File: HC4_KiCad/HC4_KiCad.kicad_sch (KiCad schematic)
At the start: 17 parts, among them IC1 KM62256CLP, IC2 ROM, J1 Power, J2 ~{CE}_EXT, SW1 SW_SPDT_312

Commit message: 基板ぬ
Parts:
- IC1: footprint Package_DIP:DIP-28_W15.24mm -> Package_SO:SOP-28_8.4x18.16mm_P1.27mm
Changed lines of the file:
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@@
 			)
 		)
-		(property "Footprint" "Package_DIP:DIP-28_W15.24mm"
+		(property "Footprint" "Package_SO:SOP-28_8.4x18.16mm_P1.27mm"
 			(at 48.26 85.09 0)
 			(effects

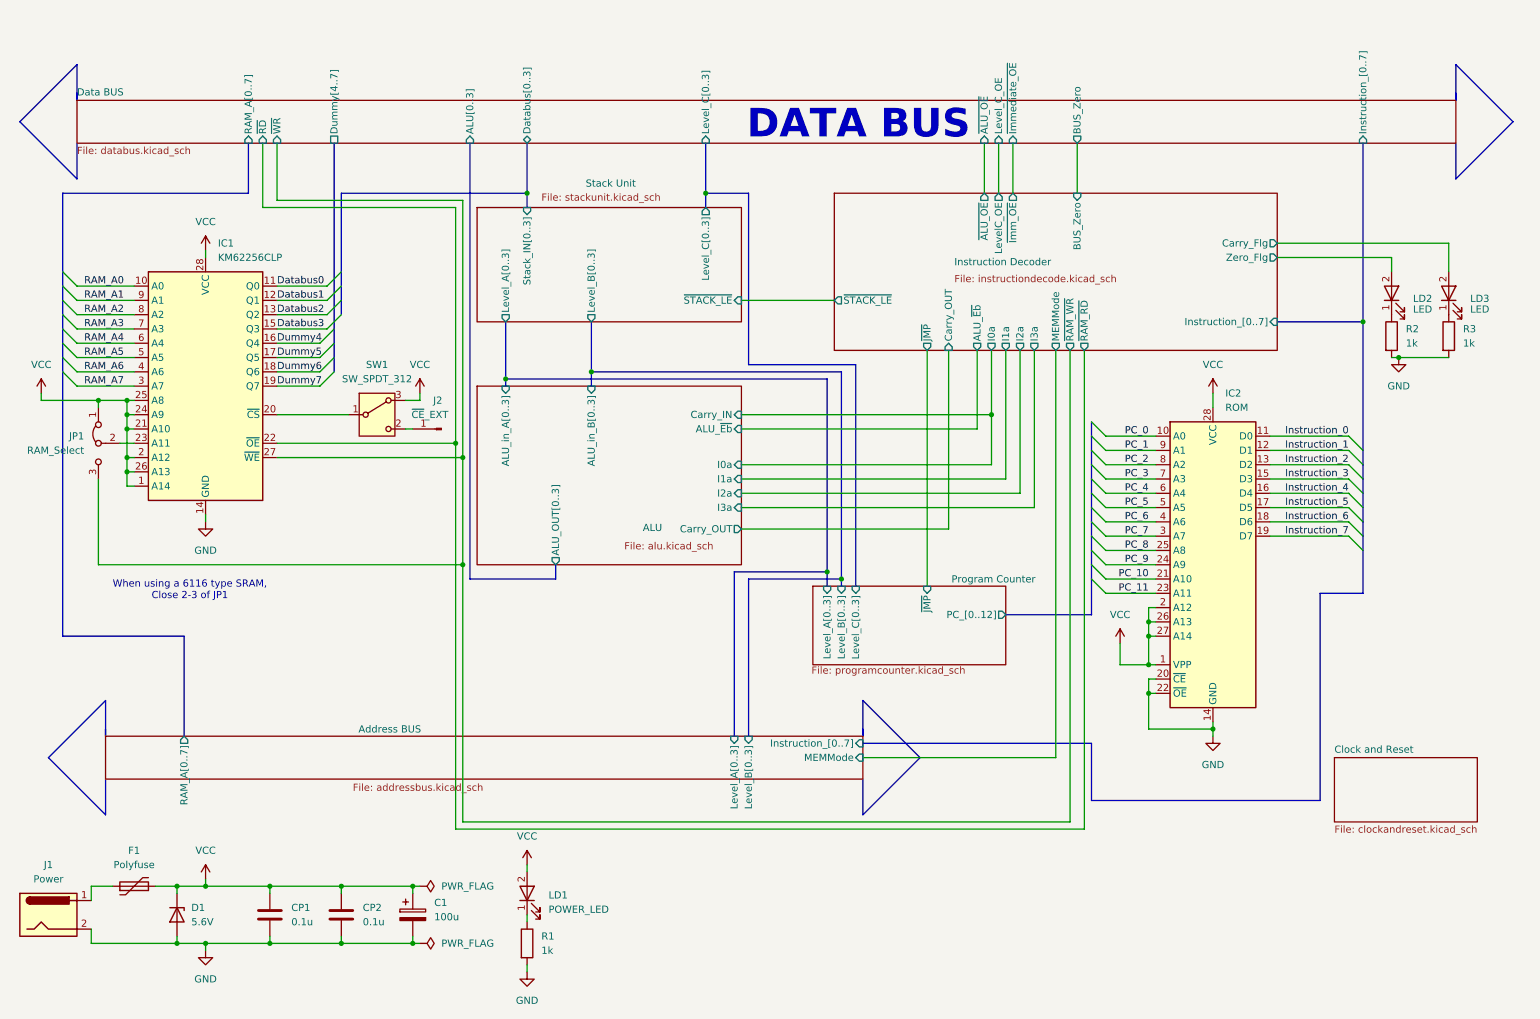
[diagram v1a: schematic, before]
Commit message: Added output port for blink
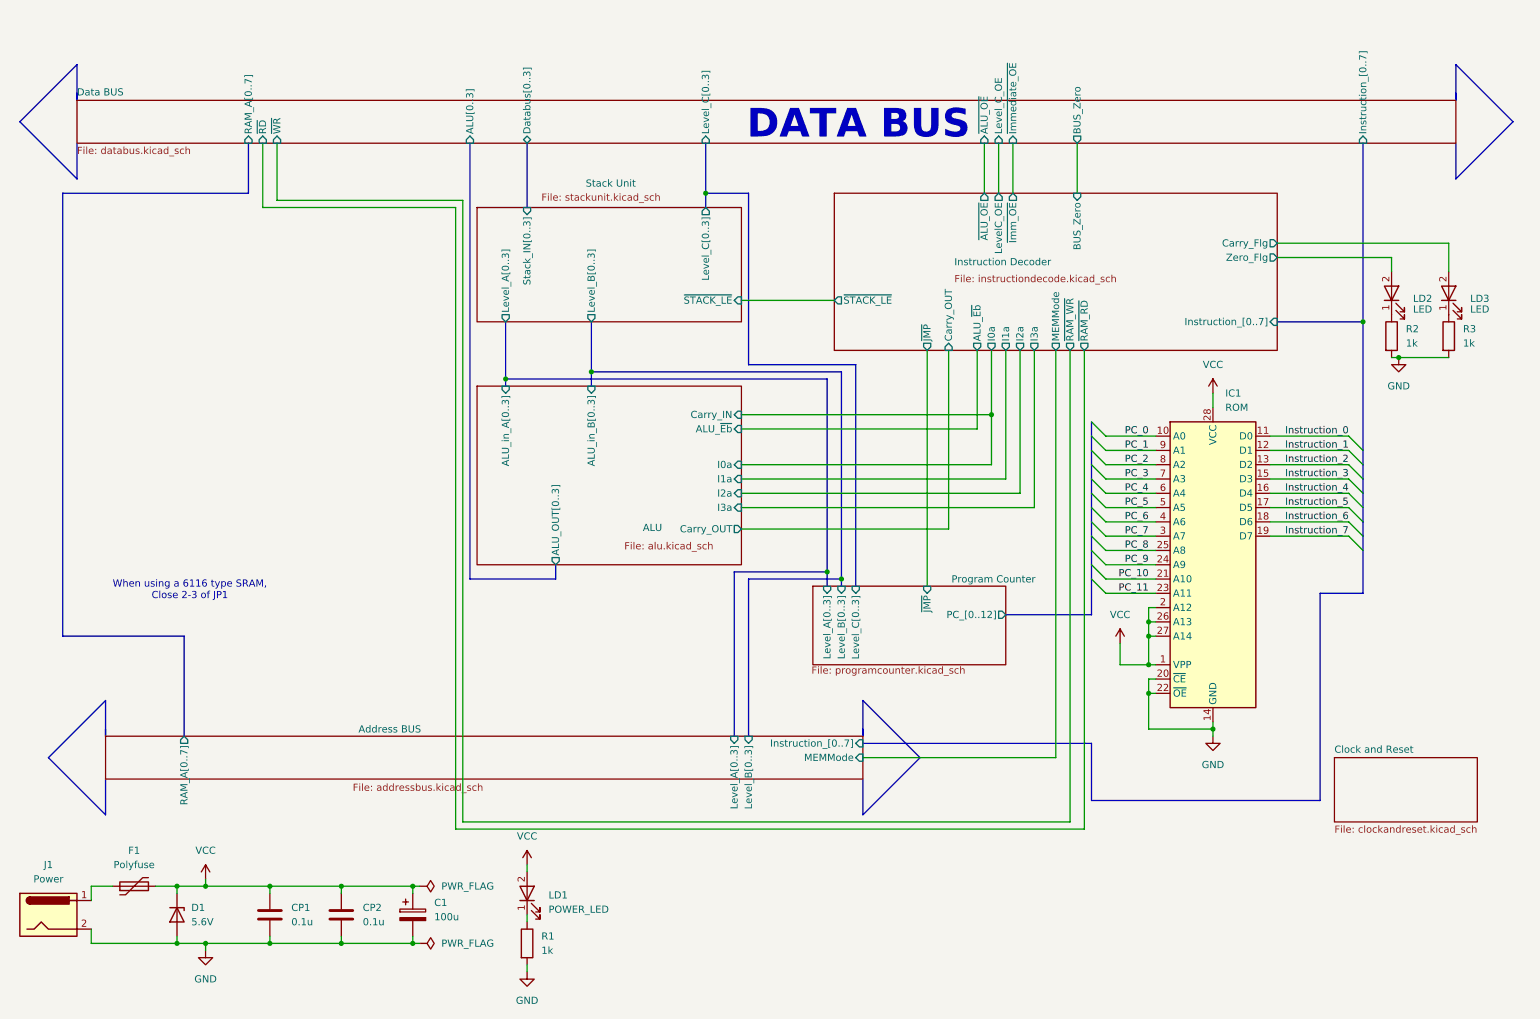
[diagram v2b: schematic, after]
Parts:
- removed IC1: KM62256CLP, Package_SO:SOP-28_8.4x18.16mm_P1.27mm, symbol Memory_RAM:KM62256CLP
- removed J2: ~{CE}_EXT, Connector_PinHeader_2.54mm:PinHeader_1x01_P2.54mm_Vertical, symbol Connector:Conn_01x01_Pin
- removed JP1: RAM_Select, Connector_PinHeader_2.54mm:PinHeader_1x03_P2.54mm_Vertical, symbol Jumper:Jumper_3_Bridged12
- removed SW1: SW_SPDT_312, Button_Switch_THT:SW_Slide-03_Wuerth-WS-SLTV_10x2.5x6.4_P2.54mm, symbol Switch:SW_SPDT_312
- renumbered IC2 to IC1
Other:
- sheet Data BUS ports: added none; removed Dummy[4..7]
